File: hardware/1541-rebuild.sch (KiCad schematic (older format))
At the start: 3 parts, among them IC1 ATMEGA1284P-P, X1 20Mhz

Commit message: Weiter am Schaltplan gezeichnet ... noch sehr Fehlerhaft
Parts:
- added C1, C2: 100n, symbol C
- added P1: CONN_01X02, symbol CONN_01X02
- added P?: 1541_CN3, symbol CONN_01X06
- added P?: 1541_VIA2_DATEN_PORT_A, symbol CONN_01X08
- added R1: 10k, symbol R
- renumbered C1 to C3
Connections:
- net +5V: now also C1.1, C2.1, P1.1 (P1), R1.2
- net GND: now also C1.2, C2.2, P1.2 (P2)
- net at IC1.1 ((PCINT8/T0/XCK)PB0): now also P?.3 (P3)
- net at IC1.14 ((PCINT24/RXD0)PD0): now also P?.1 (P1)
- net at IC1.15 ((PCINT25/TXD0)PD1): now also P?.2 (P2)
- net at IC1.16 ((PCINT26/RXD1/INT0)PD2): now also P?.3 (P3)
- net at IC1.17 ((PCINT27/TXD1/INT1)PD3): now also P?.4 (P4)
- net at IC1.18 ((PCINT28/XCK1/OC1B)PD4): now also P?.5 (P5)
- net at IC1.19 ((PCINT294/OC1A)PD5): now also P?.6 (P6)
- net at IC1.2 ((PCINT9/CLKO/T1)PB1): now also P?.4 (P4)
- net at IC1.20 ((PCINT30/OC2B/ICP)PD6): now also P?.7 (P7)
- net at IC1.21 ((PCINT31/OC2A)PD7): now also P?.8 (P8)
- net at IC1.3 ((PCINT10/AIN0/INT2)PB2): now also P?.5 (P5)
- net at IC1.4 ((PCINT11/AIN1/OC0)PB3): now also P?.6 (P6)
- net at IC1.9 (~RESET): now also R1.1
- net MISO renamed SD Karte/MISO
- net MOSI renamed SD Karte/MOSI
- net SCK renamed SD Karte/SCK
- net SS renamed VIA2_PIN12_PB2
- no-connect marks 2 -> 3
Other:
- note added: "Am meiner 1541II Platine (ASSY ???) habe ich folgende modifiktionen durchgeführt:\n- PIN 40 von U10 (Gate Array 251828) von Platine getrennt (BYTE READY)\n- U8 (VIA 6522) ausgelötet und gesockelt\n- Dauerläufer behoben durch trennen einer Leiterbahn (genauer beschreiben)"
- note added: "Kann nicht so sein\nSD Karte und MOTOR Status\nan einem PIN"
- note added: "Noch abgleichen !!"
- note added: "Spannungsversorgung"
- note added: "Stützkondensatoren für IC1"
- note removed: "Am meinem 1541II Board sind folgende modifiktionen durchgeführt worden:\n- PIN 40 von U10 (Gate Array 251828) von Platine getrennt (BYTE READY)\n- U8 (VIA 6522) ausgelötet und gesockelt\n- Dauerläufer behoben durch trennen einer Leiterbahn (genauer beschreiben)"
- moved on the sheet: C3, IC1, X1

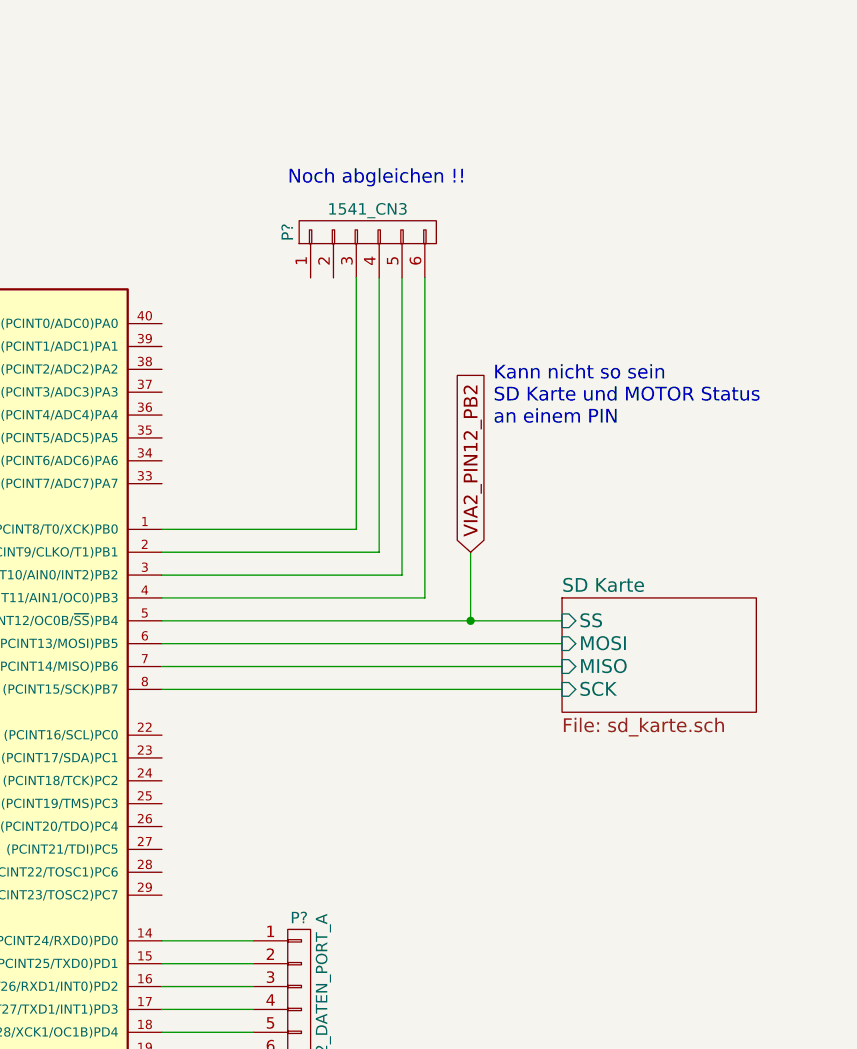
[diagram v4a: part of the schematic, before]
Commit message: Schaltplan angepasst.Motor von PortA auf PortC verlegt.
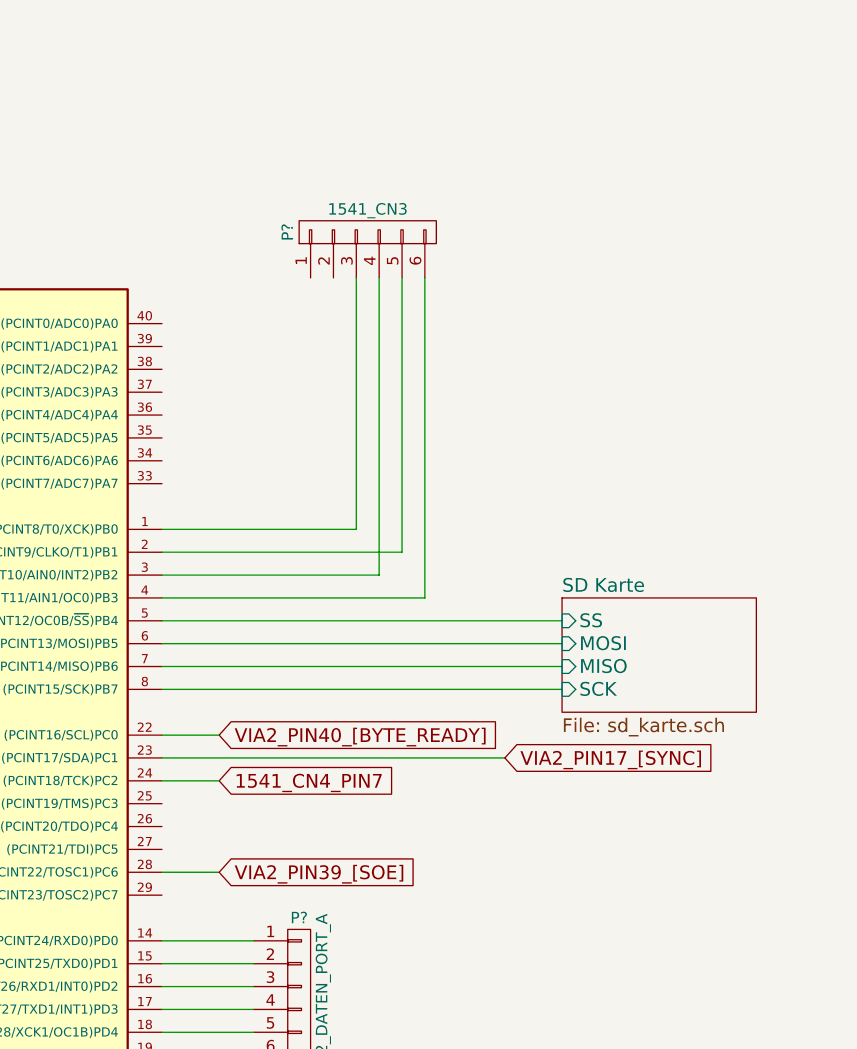
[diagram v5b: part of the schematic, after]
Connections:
- net at IC1.2 ((PCINT9/CLKO/T1)PB1): now also P?.5 (P5); no longer P?.4 (P4)
- net VIA2_PIN40_[BYTE_READY]: now reaches IC1.22 ((PCINT16/SCL)PC0)
- net VIA2_PIN17_[SYNC]: now reaches IC1.23 ((PCINT17/SDA)PC1)
- net 1541_CN4_PIN7: now reaches IC1.24 ((PCINT18/TCK)PC2)
- net VIA2_PIN39_[SOE]: now reaches IC1.28 ((PCINT22/TOSC1)PC6)
- net at IC1.3 ((PCINT10/AIN0/INT2)PB2): now also P?.4 (P4); no longer P?.5 (P5)
- net VIA2_PIN12_PB2 renamed SD Karte/SS
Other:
- note removed: "Kann nicht so sein\nSD Karte und MOTOR Status\nan einem PIN"
- note removed: "Noch abgleichen !!"
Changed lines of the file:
@@
 Wire Wire Line
 	2800 1200 2800 1350
-Wire Wire Line
-	7450 3400 7450 3100
-Connection ~ 7450 3400
-Text GLabel 7450 3100 1    60   Input ~ 0
-VIA2_PIN12_PB2
-Text Notes 7550 2550 0    60   ~ 0
-Kann nicht so sein\nSD Karte und MOTOR Status\nan einem PIN
 $Comp
 L CONN_01X06 P?
@@
 Wire Wire Line
 	6950 3000 6100 3000
-Wire Wire Line
-	7050 1900 7050 3100
-Wire Wire Line
-	7050 3100 6100 3100
-Wire Wire Line
-	7150 1900 7150 3200
-Wire Wire Line
-	7150 3200 6100 3200
-Wire Wire Line
-	7250 1900 7250 3300
-Wire Wire Line
-	7250 3300 6100 3300
-Text Notes 6650 1500 0    60   ~ 0
-Noch abgleichen !!
 $Comp
 L CONN_01X08 P?
@@
 Wire Wire Line
 	6500 5500 6100 5500
+Text GLabel 6350 4100 2    60   Input ~ 0
+1541_CN4_PIN7
+Wire Wire Line
+	6100 4100 6350 4100
+Wire Wire Line
+	6100 3100 7150 3100
+Wire Wire Line
+	7150 3100 7150 1900
+Wire Wire Line
+	6100 3200 7050 3200
+Wire Wire Line
+	7050 3200 7050 1900
+Wire Wire Line
+	6100 3300 7250 3300
+Wire Wire Line
+	7250 3300 7250 1900
+Wire Wire Line
+	6100 3900 6350 3900
+Text GLabel 6350 3900 2    60   Input ~ 0
+VIA2_PIN40_[BYTE_READY]
+Wire Wire Line
+	6100 4000 7600 4000
+Text GLabel 7600 4000 2    60   Input ~ 0
+VIA2_PIN17_[SYNC]
+Wire Wire Line
+	6100 4500 6350 4500
+Text GLabel 6350 4500 2    60   Input ~ 0
+VIA2_PIN39_[SOE]
 $EndSCHEMATC
